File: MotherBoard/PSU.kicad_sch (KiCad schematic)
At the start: 0 parts

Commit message: PSU Complete
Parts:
- added C401, C402: C, symbol Device:C
- added C403, C404, C405, C406, C412, C413: 1u, symbol Device:C
- added C407, C408, C409, C414: 100n, symbol Device:C
- added C410, C411: 47u, symbol Device:C
- added D401, D402: GREEN, symbol Device:LED
- added L401: L, symbol Device:L
- added L402, L403: 22u, SW_Inductor:IND_IHLP-6767DZ_VIS, symbol Device:L
- added R401: 100k, Resistor_SMD:R_0402_1005Metric, symbol Device:R_US
- added R402, R404: 22.1k, Resistor_SMD:R_0402_1005Metric, symbol Device:R_US
- added R403: 162k, Resistor_SMD:R_0402_1005Metric, symbol Device:R_US
- added R405, R406: 1k, Resistor_SMD:R_0402_1005Metric, symbol Device:R_US
- added U401, U402: LMR51430, Package_TO_SOT_SMD:SOT-23-6, symbol Regulator_Switching:LMR51430
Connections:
- new net: D402.1 (K), R406.1
- new net: D401.1 (K), R405.1
- new net +12V: C402.1, C403.1, C404.1, C405.1, C406.1, C407.1, C412.1, C413.1, C414.1, L401.2, U401.3 (VIN), U401.5 (EN), U402.3 (VIN), U402.5 (EN)
- new net +3V3: C410.1, D401.2 (A), L402.2, R401.1
- new net +5V: C411.1, D402.2 (A), L403.2, R403.1
- new net BUCK_FB_3V3: R401.2, R402.1, U401.4 (FB)
- new net BUCK_FB_5V: R403.2, R404.1, U402.4 (FB)
- new net BUCK_SW_3V3: C408.2, L402.1, U401.2 (SW)
- new net BUCK_SW_5V: C409.2, L403.1, U402.2 (SW)
- new net CBOOT_3V3: C408.1, U401.6 (CB)
- new net CBOOT_5V: C409.1, U402.6 (CB)
- new net GND: C401.2, C402.2, C403.2, C404.2, C405.2, C406.2, C407.2, C410.2, C411.2, C412.2, C413.2, C414.2, R402.2, R404.2, R405.2, R406.2, U401.1 (GND), U402.1 (GND)
- new net VBUS: C401.1, L401.1
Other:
- note added: "Both Regulators f(sw) = 1.1Mhz I(load) = 3A Max"
- note added: "DCR = ? I(max) = ?"
- note added: "PI Filter in MHZ Range Set inductor current rating for Imax"
- note added: "f(sw) = 1.1Mhz I(load) = 3A Max"
- note added: "https://www.ti.com/product/LMR51430/part-details/LMR51430YDDCR https://www.digikey.com/en/products/detail/vishay-dale/IHLP6767DZER220M11/2533938"

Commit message: Fixed CAN tranceivers + added relay driver circuit + fixed relative file paths for 3D models + finished PSU but still need correct 3D model
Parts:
- C401, C402: value C -> 100n
- L401: value L -> 10n
- renumbered C406 to C403, C403 to C404, C412 to C405, C404 to C406, C413 to C407, C405 to C408, C414 to C409, C407 to C410, C408 to C411, C409 to C412, C410 to C413, C411 to C414
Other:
- note added: "5 MHz cutoff"
- note added: "DCR = 0R15 I(max) = 2A"
- note removed: "DCR = ? I(max) = ?"
- note removed: "PI Filter in MHZ Range Set inductor current rating for Imax"
- moved on the sheet: C401, C402, C403, C404, C405, C406, C407, C408, C409, C410, C411, C412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

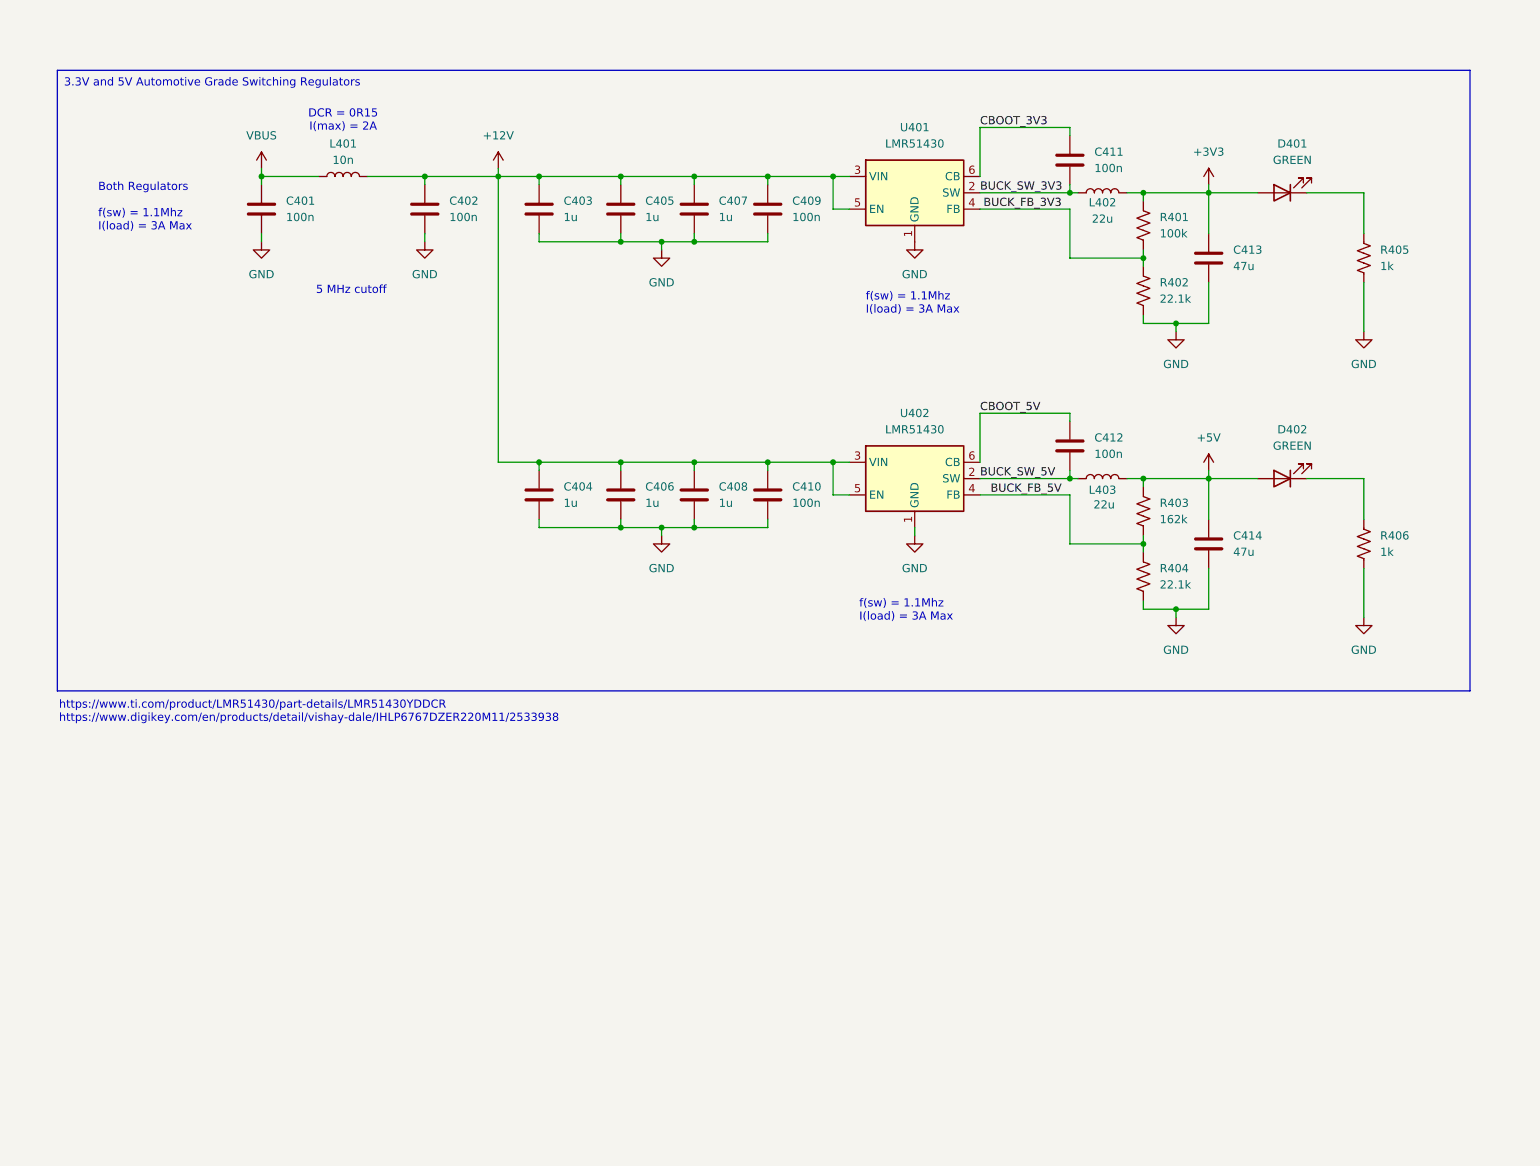
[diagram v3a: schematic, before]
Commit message: Revised all schematics + completed relay driver page
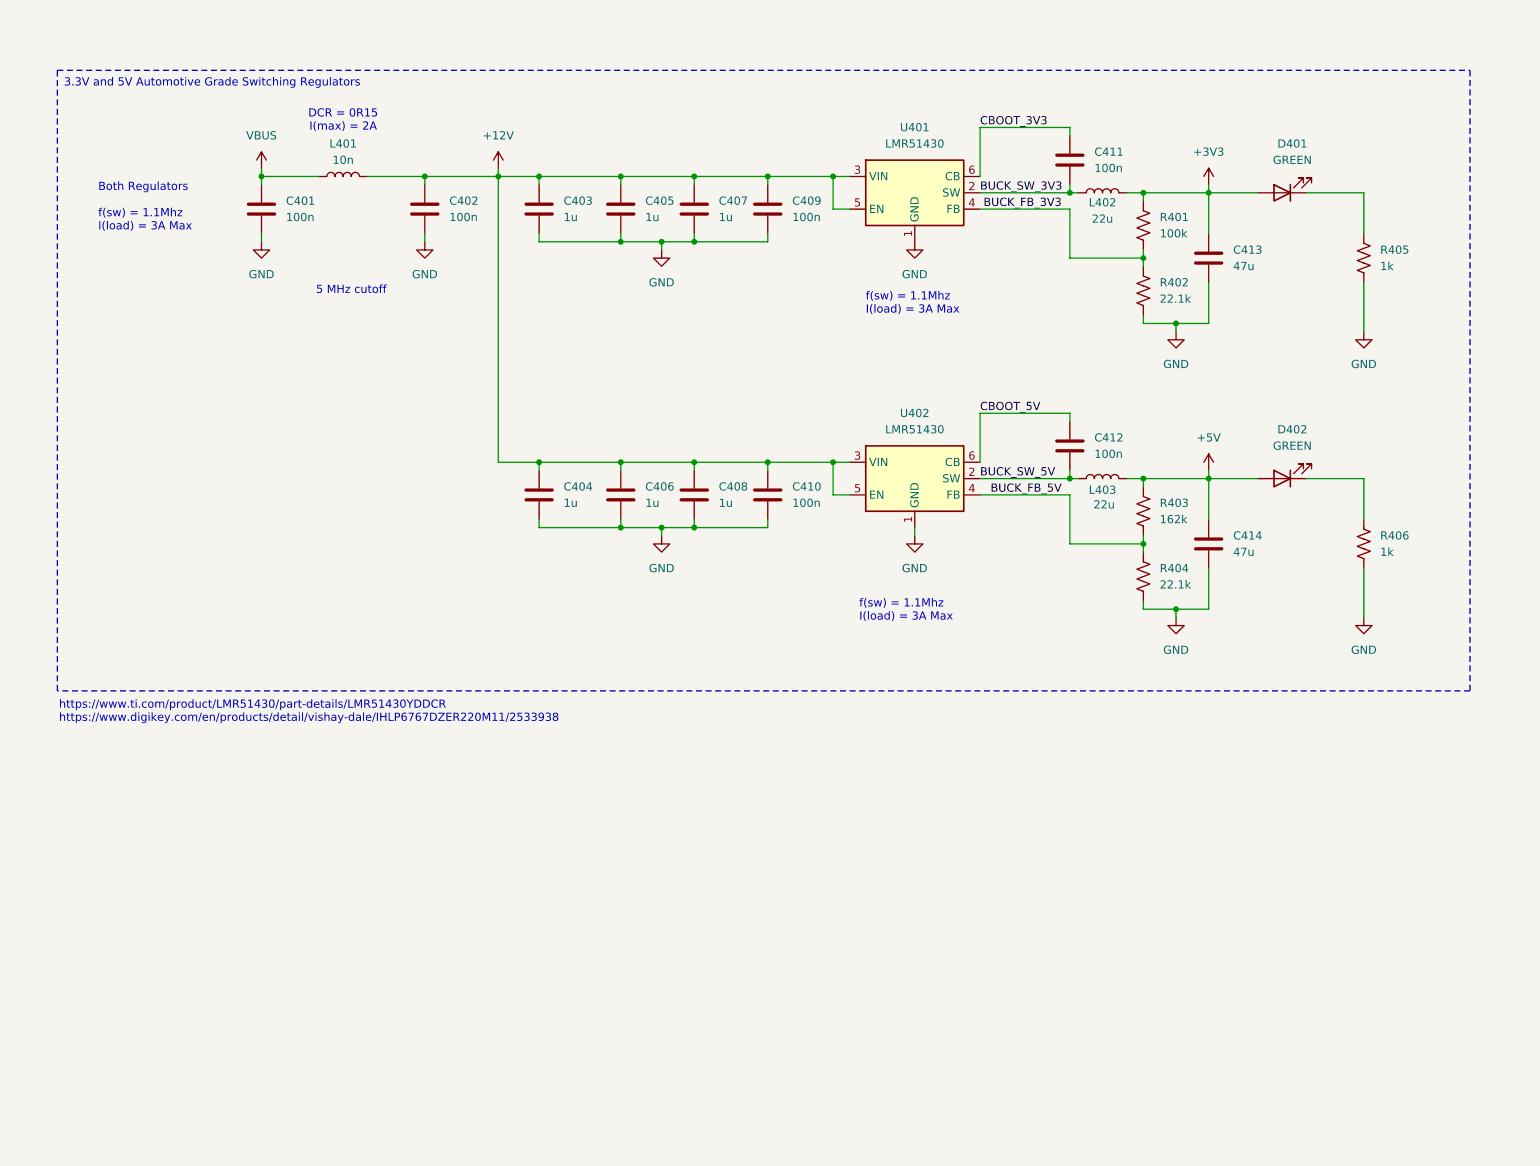
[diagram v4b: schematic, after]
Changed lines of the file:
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@@
 	(title_block
 		(title "STM32 Layout")
-		(date "2025-01-08")
+		(date "2025-01-10")
 		(rev "A")
 		(company "FSAE LSU")
@@
 		(stroke
 			(width 0)
-			(type default)
+			(type dash)
 		)
 		(fill

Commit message: Fixed 3D model paths. Finished PSU ORing shcematic.
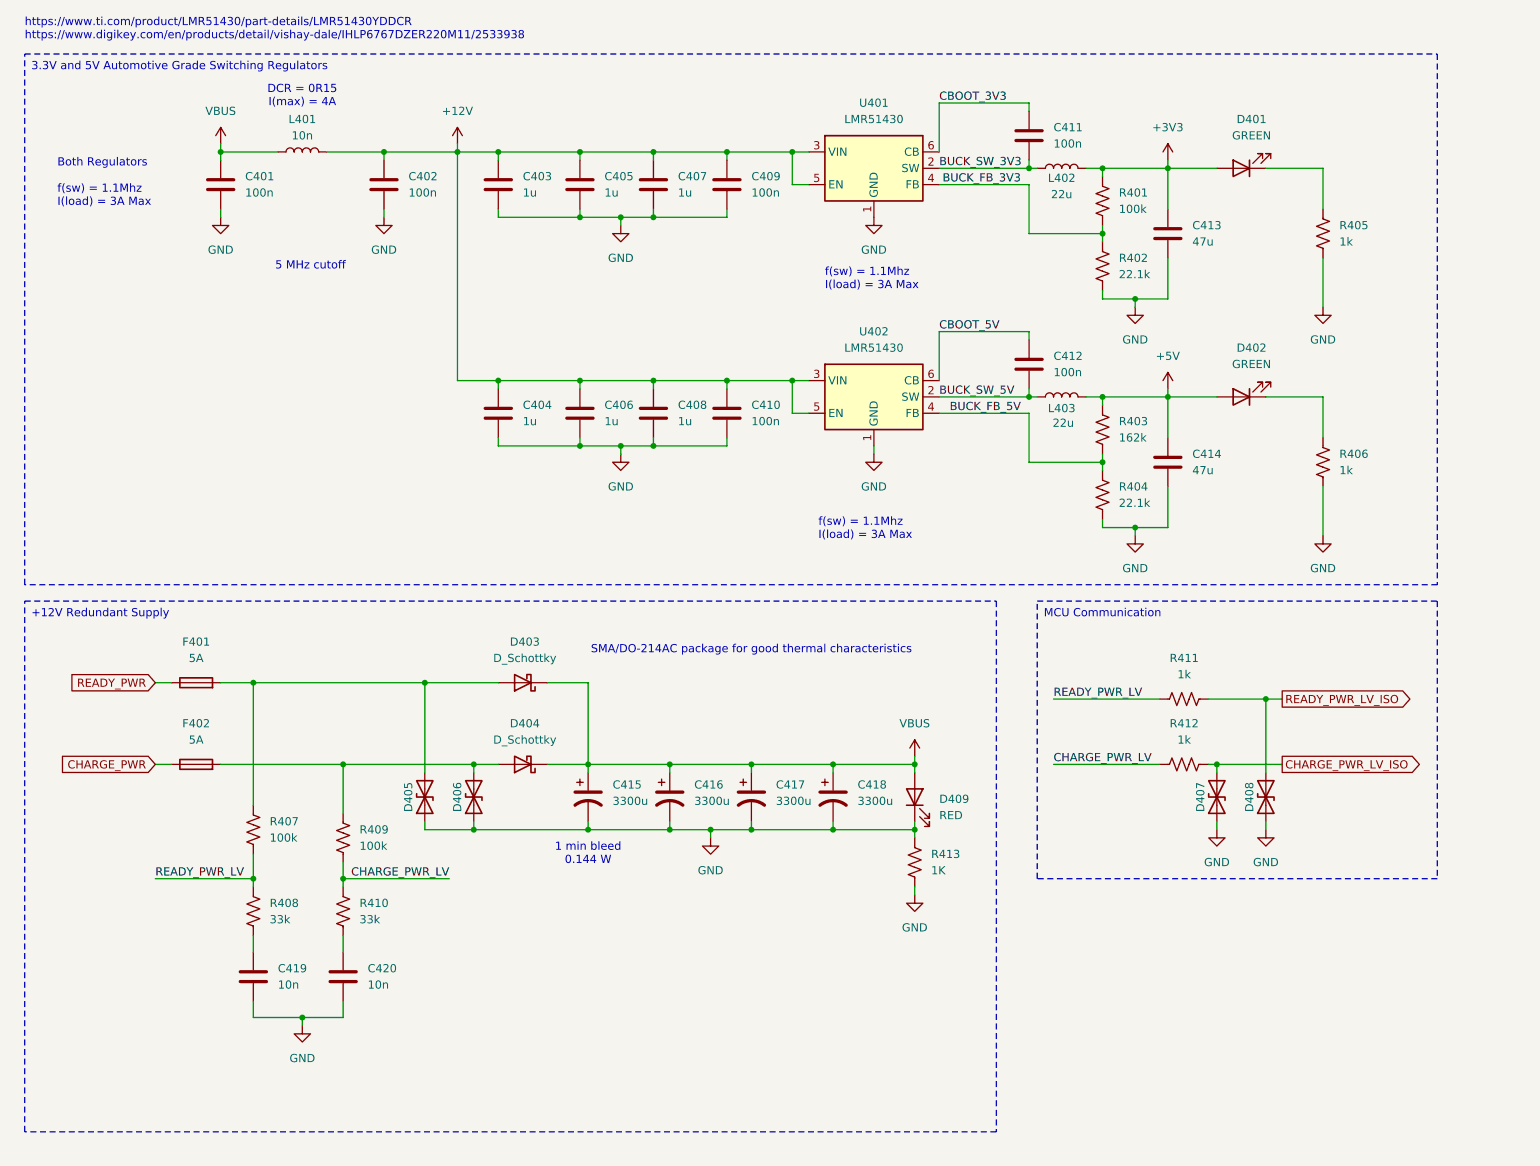
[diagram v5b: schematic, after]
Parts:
- added C415, C416, C417, C418: 3300u, symbol Device:C_Polarized_US
- added C419, C420: 10n, symbol Device:C
- added D403, D404: D_Schottky, symbol Device:D_Schottky
- added D405, D406, D407, D408: D_TVS, Diode_SMD:D_SOD-323, symbol Device:D_TVS
- added D409: RED, symbol Device:LED
- added F401, F402: 5A, symbol Device:Fuse
- added R407, R409: 100k, Resistor_SMD:R_0402_1005Metric, symbol Device:R_US
- added R408, R410: 33k, Resistor_SMD:R_0402_1005Metric, symbol Device:R_US
- added R411, R412: 1k, Resistor_SMD:R_0402_1005Metric, symbol Device:R_US
- added R413: 1K, Resistor_SMD:R_0402_1005Metric, symbol Device:R_US
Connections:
- net GND: now also C415.2, C416.2, C417.2, C418.2, C419.2, C420.2, D405.1 (A1), D406.1 (A1), D407.1 (A1), D408.1 (A1), D409.1 (K), R413.1, R413.2
- net VBUS: now also C415.1, C416.1, C417.1, C418.1, D403.1 (K), D404.1 (K), D409.2 (A)
- new net: C419.1, R408.2
- new net: D404.2 (A), D406.2 (A2), F402.2, R409.1
- new net: C420.1, R410.2
- new net: D403.2 (A), D405.2 (A2), F401.2, R407.1
- new net CHARGE_PWR: F402.1
- new net CHARGE_PWR_LV: R409.2, R410.1, R412.1
- new net CHARGE_PWR_LV_ISO: D407.2 (A2), R412.2
- new net READY_PWR: F401.1
- new net READY_PWR_LV: R407.2, R408.1, R411.1
- new net READY_PWR_LV_ISO: D408.2 (A2), R411.2
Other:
- note added: "1 min bleed 0.144 W"
- note added: "DCR = 0R15 I(max) = 4A"
- note added: "SMA/DO-214AC package for good thermal characteristics"
- note removed: "DCR = 0R15 I(max) = 2A"
- moved on the sheet: C401, C402, C403, C404, C405, C406, C407, C408, C409, C410, C411, C412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

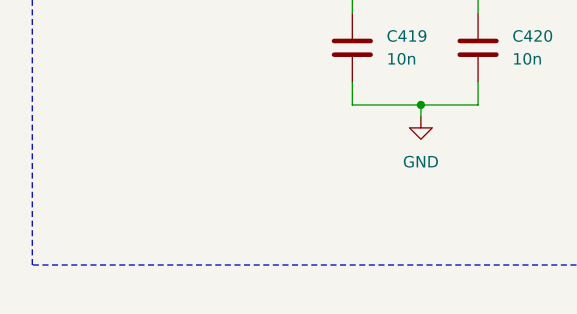
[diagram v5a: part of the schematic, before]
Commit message: Added more 3D models
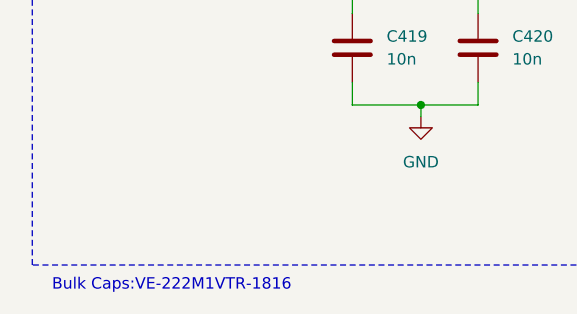
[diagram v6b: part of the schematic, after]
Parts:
- C401, C402, C403, C404, C405, C406, C407, C408, C409, C410, C411, C412, C413, C414, C419, C420, L401: footprint (none) -> Capacitor_SMD:C_0402_1005Metric
- C415, C416, C417, C418: footprint (none) -> Capacitor_SMD:CP_Elec_18x17.5
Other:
- note added: "Bulk Caps:VE-222M1VTR-1816"
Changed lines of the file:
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@@
 		)
 	)
+	(text "Bulk Caps:VE-222M1VTR-1816"
+		(exclude_from_sim no)
+		(at 35.814 192.786 0)
+		(effects
+			(font
+				(size 1.27 1.27)
+			)
+		)
+	)
 	(text "5 MHz cutoff\n"
 		(exclude_from_sim no)
@@
 			)
 		)
-		(property "Footprint" ""
+		(property "Footprint" "Capacitor_SMD:CP_Elec_18x17.5"
 			(at 146.05 138.43 0)
 			(effects
@@
 			)
 		)
-		(property "Footprint" ""
+		(property "Footprint" "Capacitor_SMD:C_0402_1005Metric"
 			(at 199.0852 90.17 0)
 			(effects
@@
 			)
 		)
-		(property "Footprint" ""
+		(property "Footprint" "Capacitor_SMD:C_0402_1005Metric"
 			(at 119.0752 82.55 0)
 			(effects
@@
 			)
 		)
-		(property "Footprint" ""
+		(property "Footprint" "Capacitor_SMD:C_0402_1005Metric"
 			(at 177.4952 39.37 0)
 			(effects
@@
 			)
 		)
-		(property "Footprint" ""
+		(property "Footprint" "Capacitor_SMD:C_0402_1005Metric"
 			(at 94.9452 82.55 0)
 			(effects
@@
 			)
 		)
-		(property "Footprint" ""
+		(property "Footprint" "Capacitor_SMD:C_0402_1005Metric"
 			(at 177.4952 74.93 0)
 			(effects
@@
 			)
 		)
-		(property "Footprint" ""
+		(property "Footprint" "Capacitor_SMD:CP_Elec_18x17.5"
 			(at 107.95 138.43 0)
 			(effects
@@
 			)
 		)
-		(property "Footprint" ""
+		(property "Footprint" "Capacitor_SMD:C_0402_1005Metric"
 			(at 130.5052 82.55 0)
 			(effects
@@
 			)
 		)
-		(property "Footprint" ""
+		(property "Footprint" "Capacitor_SMD:CP_Elec_18x17.5"
 			(at 120.65 138.43 0)
 			(effects
@@
 			)
 		)
-		(property "Footprint" ""
+		(property "Footprint" "Capacitor_SMD:C_0402_1005Metric"
 			(at 107.6452 82.55 0)
 			(effects
@@
 			)
 		)
-		(property "Footprint" ""
+		(property "Footprint" "Capacitor_SMD:C_0402_1005Metric"
 			(at 199.0852 54.61 0)
 			(effects
@@
 			)
 		)
-		(property "Footprint" ""
+		(property "Footprint" "Capacitor_SMD:C_0402_1005Metric"
 			(at 70.8152 170.18 0)
 			(effects
@@
 			)
 		)
-		(property "Footprint" ""
+		(property "Footprint" "Capacitor_SMD:C_0402_1005Metric"
 			(at 51.7652 46.99 0)
 			(effects
@@
 			)
 		)
-		(property "Footprint" ""
+		(property "Footprint" "Capacitor_SMD:C_0402_1005Metric"
 			(at 119.0752 46.99 0)
 			(effects
@@
 			)
 		)
-		(property "Footprint" ""
+		(property "Footprint" "Capacitor_SMD:C_0402_1005Metric"
 			(at 94.9452 46.99 0)
 			(effects
@@
 			)
 		)
-		(property "Footprint" ""
+		(property "Footprint" "Capacitor_SMD:C_0402_1005Metric"
 			(at 130.5052 46.99 0)
 			(effects
@@
 			)
 		)
-		(property "Footprint" ""
+		(property "Footprint" "Capacitor_SMD:CP_Elec_18x17.5"
 			(at 133.35 138.43 0)
 			(effects
@@
 			)
 		)
-		(property "Footprint" ""
+		(property "Footprint" "Capacitor_SMD:C_0402_1005Metric"
 			(at 56.8452 170.18 0)
 			(effects
@@
 			)
 		)
-		(property "Footprint" ""
+		(property "Footprint" "Capacitor_SMD:C_0402_1005Metric"
 			(at 107.6452 46.99 0)
 			(effects
@@
 			)
 		)
-		(property "Footprint" ""
+		(property "Footprint" "Capacitor_SMD:C_0402_1005Metric"
 			(at 63.5 38.1 0)
 			(effects
@@
 			)
 		)
-		(property "Footprint" ""
+		(property "Footprint" "Capacitor_SMD:C_0402_1005Metric"
 			(at 77.1652 46.99 0)
 			(effects

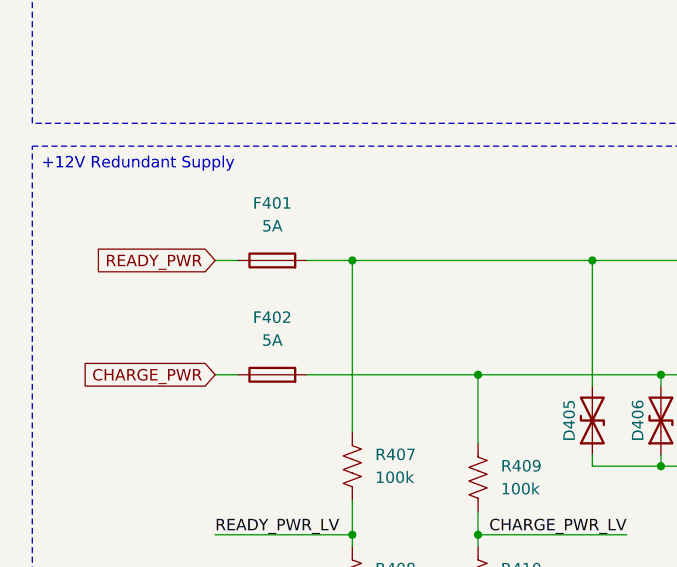
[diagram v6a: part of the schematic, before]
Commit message: Fixed relative paths + 90% footprints done + organized PCB for layout + found JLC part #s for manufacturing
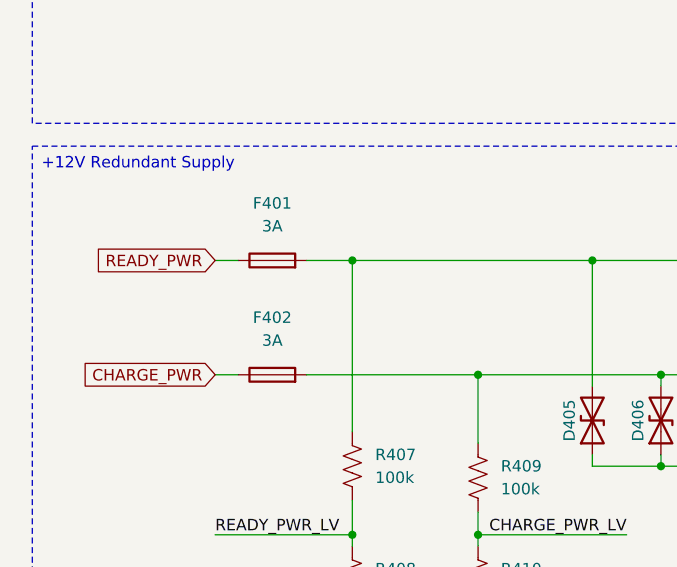
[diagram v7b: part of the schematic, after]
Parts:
- D401, D402, D409: footprint (none) -> LED_SMD:LED_0603_1608Metric
- D403, D404: footprint (none) -> Diode_SMD:D_SMA; Manufacturer_Part_Number (none) -> SS54
- F401, F402: value 5A -> 3A; footprint (none) -> Fuse:Fuse_1206_3216Metric; Manufacturer_Part_Number (none) -> 12H1300C
- L402, L403: footprint SW_Inductor:IND_IHLP-6767DZ_VIS -> Inductor_SMD:L_Changjiang_FNR6045S; Manufacturer_Part_Number (none) -> FNR6045S220MT
- U401, U402: Manufacturer_Part_Number (none) -> LMR51430YDDCR
